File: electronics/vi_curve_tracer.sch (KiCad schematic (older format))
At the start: 56 parts, among them P1 CONN_01X05, P2 USB_OTG, P3 CONN_01X03, P4 CONN_01X03, U1 MCP6004, U2 pic24f08km202, U3 ft230x

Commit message: Fixes #8 - Added ground reference on the terminal block
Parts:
- removed P3: CONN_01X03, kicad_pcb:CONN_1x3_OSTTC032162, symbol CONN_01X03
- removed P4: CONN_01X03, kicad_pcb:CONN_2x3_SOCKET, symbol CONN_01X03
- added P3: CONN_01X04, kicad_pcb:CONN_1x4_OSTTC042162, symbol CONN_01X04
- added P4: CONN_01X06, kicad_pcb:CONN_2x3_SOCKET, symbol CONN_01X06
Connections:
- net GNDD: now also P3.1 (P1)
- net GateVoltage: now also P3.2 (P2), P4.1 (P1), P4.6 (P6)
- net LD_VOLTAGE_0: now also P3.3 (P3), P4.2 (P2), P4.4 (P4)
- net LD_VOLTAGE_1: now also P3.4 (P4), P4.3 (P3), P4.5 (P5)
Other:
- note added: "D"
- note added: "G"
- note added: "S"
- note removed: "TO-220 Socket\nMay want to add extra sockets for different arrangements"
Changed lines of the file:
@@
 encoding utf-8
 Sheet 1 1
-Title ""
-Date ""
-Rev ""
-Comp ""
+Title "Curve Tracer"
+Date "2016-06-06"
+Rev "1.0"
+Comp "for(embed)"
 Comment1 ""
 Comment2 ""
@@
 Text Notes 10200 4450 0    60   ~ 0
 Sense Resistor
-$Comp
-L CONN_01X03 P4
-U 1 1 56B3BE2B
-P 10450 3300
-F 0 "P4" H 10450 3500 50  0000 C CNN
-F 1 "CONN_01X03" V 10550 3300 50  0000 C CNN
-F 2 "kicad_pcb:CONN_2x3_SOCKET" H 10450 3300 50  0001 C CNN
-F 3 "" H 10450 3300 50  0000 C CNN
-F 4 "A06-LC-TT" H 10450 3300 60  0001 C CNN "MPN"
-F 5 "DIP socket" H 10450 3300 60  0001 C CNN "Description"
-F 6 "Assmann WSW Components" H 10450 3300 60  0001 C CNN "Manufacturer"
-	1    10450 3300
-	1    0    0    -1
-$EndComp
-$Comp
-L CONN_01X03 P3
-U 1 1 56B3C6AA
-P 10450 2600
-F 0 "P3" H 10450 2800 50  0000 C CNN
-F 1 "CONN_01X03" V 10550 2600 50  0000 C CNN
-F 2 "kicad_pcb:CONN_1x3_OSTTC032162" H 10450 2600 50  0001 C CNN
-F 3 "" H 10450 2600 50  0000 C CNN
-F 4 "On Shore Technology, Inc." H 10450 2600 60  0001 C CNN "Manufacturer"
-F 5 "terminal block, 5.08mm, 3pos" H 10450 2600 60  0001 C CNN "Description"
-F 6 "OSTTC032162" H 10450 2600 60  0001 C CNN "MPN"
-	1    10450 2600
-	1    0    0    -1
-$EndComp
-Text Notes 10150 3650 0    60   ~ 0
-TO-220 Socket\nMay want to add extra sockets for different arrangements
 Text Notes 10150 2950 0    60   ~ 0
 Screw Terminals
@@
 	4900 2400 5100 2400
 Wire Wire Line
-	7950 3200 10250 3200
+	7950 3200 10550 3200
 Wire Wire Line
 	5000 2700 5000 2750
@@
 	10050 6300 10050 4700
 Wire Wire Line
-	7550 3300 10250 3300
+	7550 3300 10550 3300
 Wire Wire Line
 	10050 2700 10050 4200
 Wire Wire Line
-	10050 3400 10250 3400
+	10050 3400 10550 3400
 Wire Wire Line
 	3850 6900 4000 6900
@@
 Connection ~ 10050 4150
 Wire Wire Line
-	10250 2700 10050 2700
+	10550 2700 10050 2700
 Connection ~ 10050 3400
 Wire Wire Line
-	10250 2600 9900 2600
+	10550 2600 9900 2600
 Wire Wire Line
 	9900 2600 9900 3300
 Connection ~ 9900 3300
 Wire Wire Line
-	10250 2500 9750 2500
+	10550 2500 9750 2500
 Wire Wire Line
 	9750 2500 9750 3200
@@
 Wire Wire Line
 	4350 4600 4450 4600
+$Comp
+L CONN_01X04 P3
+U 1 1 5755D3CE
+P 10750 2550
+F 0 "P3" H 10750 2800 50  0000 C CNN
+F 1 "CONN_01X04" V 10850 2550 50  0000 C CNN
+F 2 "kicad_pcb:CONN_1x4_OSTTC042162" H 10750 2550 50  0001 C CNN
+F 3 "" H 10750 2550 50  0000 C CNN
+F 4 "OSTTC042162" H 10750 2550 60  0001 C CNN "MPN"
+F 5 "On Shore Technology, Inc." H 10750 2550 60  0001 C CNN "Manufacturer"
+F 6 "terminal block, 5.08mm, 4pos" H 10750 2550 60  0001 C CNN "Description"
+	1    10750 2550
+	1    0    0    -1
+$EndComp
+$Comp
+L GNDD #PWR056
+U 1 1 5755DDF7
+P 10450 2400
+F 0 "#PWR056" H 10450 2150 50  0001 C CNN
+F 1 "GNDD" H 10450 2250 50  0000 C CNN
+F 2 "" H 10450 2400 50  0000 C CNN
+F 3 "" H 10450 2400 50  0000 C CNN
+	1    10450 2400
+	0    1    1    0
+$EndComp
+Wire Wire Line
+	10550 2400 10450 2400
+$Comp
+L CONN_01X06 P4
+U 1 1 5755ECF2
+P 10750 3450
+F 0 "P4" H 10750 3800 50  0000 C CNN
+F 1 "CONN_01X06" V 10850 3450 50  0000 C CNN
+F 2 "kicad_pcb:CONN_2x3_SOCKET" H 10750 3450 50  0001 C CNN
+F 3 "" H 10750 3450 50  0000 C CNN
+F 4 "A06-LC-TT" H 10750 3450 60  0001 C CNN "MPN"
+F 5 "DIP socket, 2x3" H 10750 3450 60  0001 C CNN "Description"
+F 6 "Assmann WSW Components" H 10750 3450 60  0001 C CNN "Manufacturer"
+	1    10750 3450
+	1    0    0    -1
+$EndComp
+Text Notes 10950 3250 0    60   ~ 0
+G
+Text Notes 10950 3350 0    60   ~ 0
+D
+Text Notes 10950 3450 0    60   ~ 0
+S
+Text Notes 10950 3750 0    60   ~ 0
+G
+Text Notes 10950 3650 0    60   ~ 0
+S
+Text Notes 10950 3550 0    60   ~ 0
+D
+Wire Wire Line
+	10550 3700 10250 3700
+Wire Wire Line
+	10250 3700 10250 3200
+Connection ~ 10250 3200
+Wire Wire Line
+	10550 3600 10350 3600
+Wire Wire Line
+	10350 3600 10350 3400
+Connection ~ 10350 3400
+Wire Wire Line
+	10550 3500 10450 3500
+Wire Wire Line
+	10450 3500 10450 3300
+Connection ~ 10450 3300
 $EndSCHEMATC

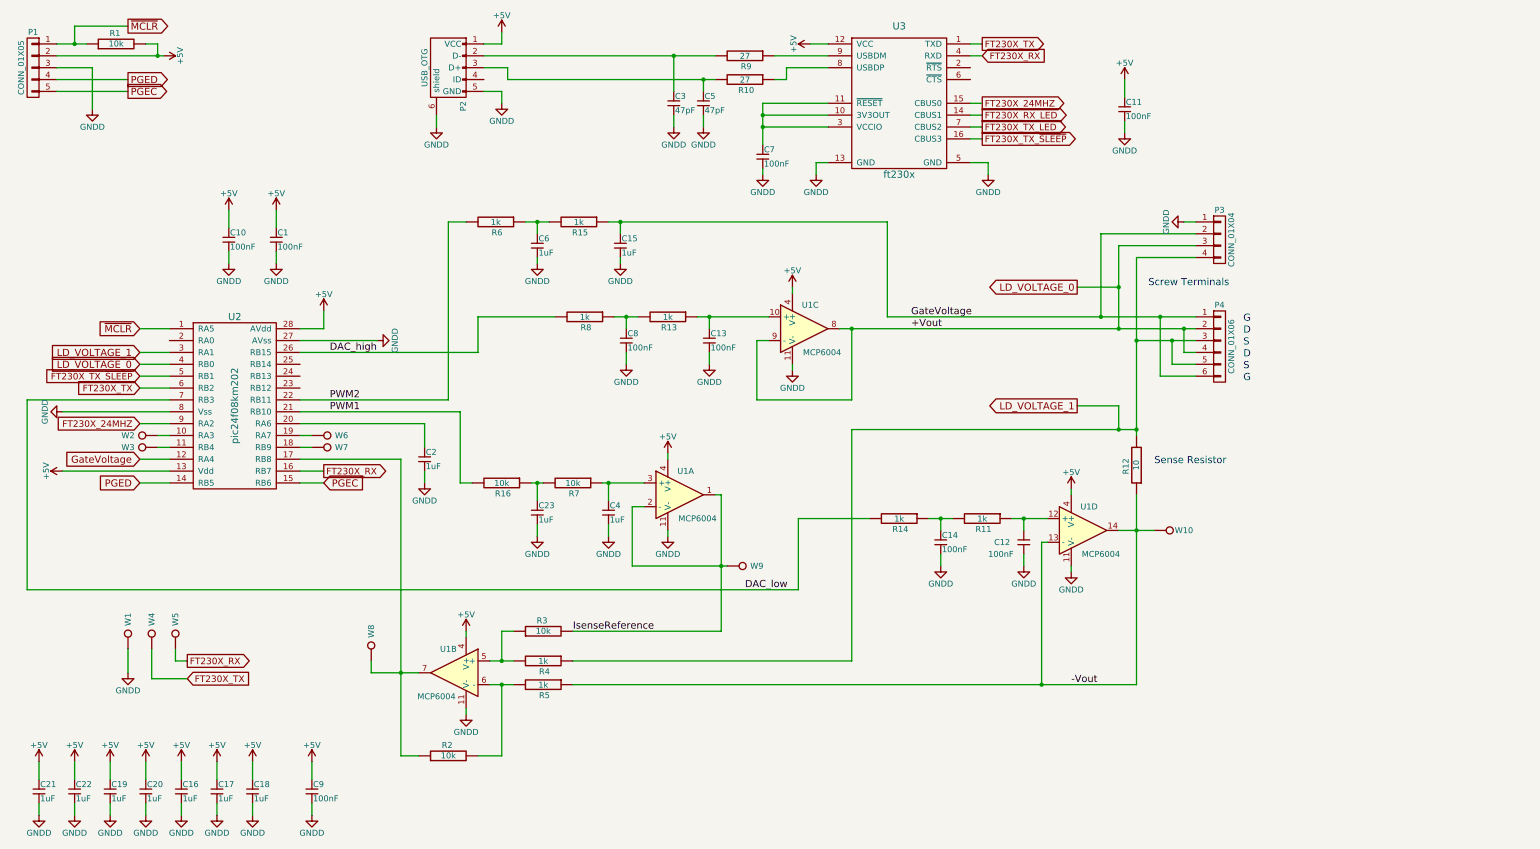
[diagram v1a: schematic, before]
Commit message: See #13 - Added XY outputs to hardware
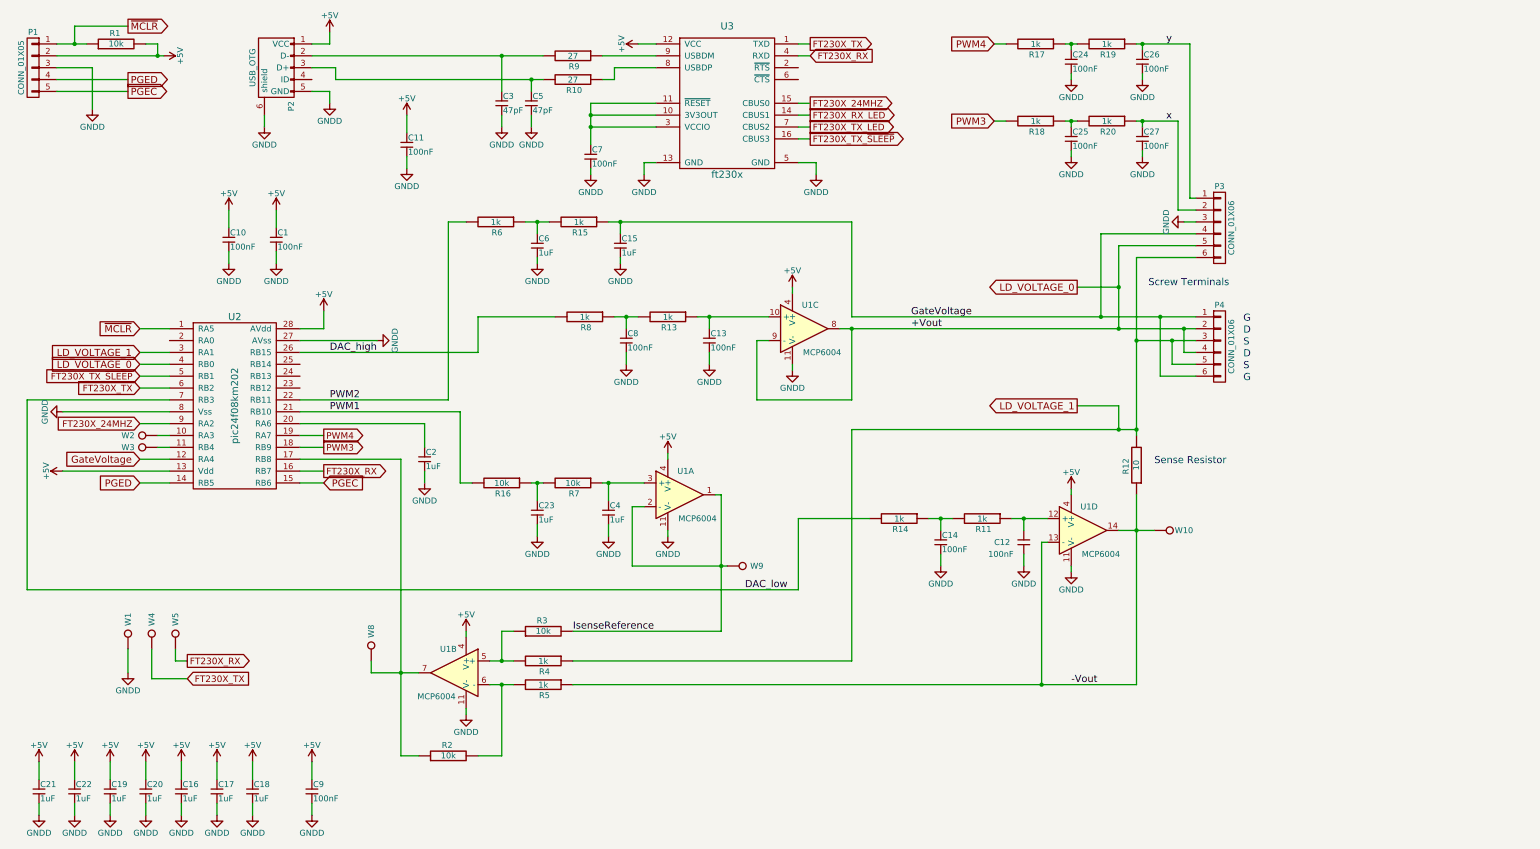
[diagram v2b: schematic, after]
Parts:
- removed P3: CONN_01X04, kicad_pcb:CONN_1x4_OSTTC042162, symbol CONN_01X04
- removed W6, W7: TEST_1P, Measurement_Points:Measurement_Point_Round-SMD-Pad_Small, symbol TEST_1P
- added C24, C25, C26, C27: 100nF, kicad_pcb:SM_0603, symbol Csmall
- added P3: CONN_01X06, kicad_pcb:CONN_1x6_OSTTC062162, symbol CONN_01X06
- added R17, R18, R19, R20: 1k, kicad_pcb:SM_0603, symbol R
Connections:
- net GNDD: now also C24.2, C25.2, C26.2, C27.2, P3.3 (P3)
- net GateVoltage: now also P3.4 (P4)
- net LD_VOLTAGE_0: now also P3.5 (P5)
- net LD_VOLTAGE_1: now also P3.6 (P6)
- net PWM3: now reaches U2.18 (RB9)
- net PWM3: now also R18.2
- net PWM4: now reaches U2.19 (RA7)
- net PWM4: now also R17.2
- new net: C24.1, R17.1, R19.2
- new net: C25.1, R18.1, R20.2
- new net x: C27.1, P3.2 (P2), R20.1
- new net y: C26.1, P3.1 (P1), R19.1
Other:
- moved on the sheet: C11, C3, C5, C7, P2, R10, R9, U3

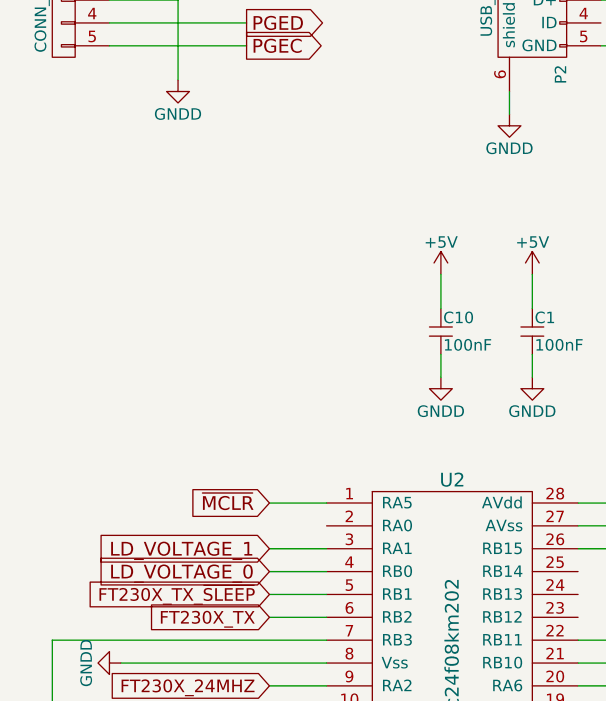
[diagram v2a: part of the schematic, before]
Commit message: Added extra header to short in case we want to add a bootloader later
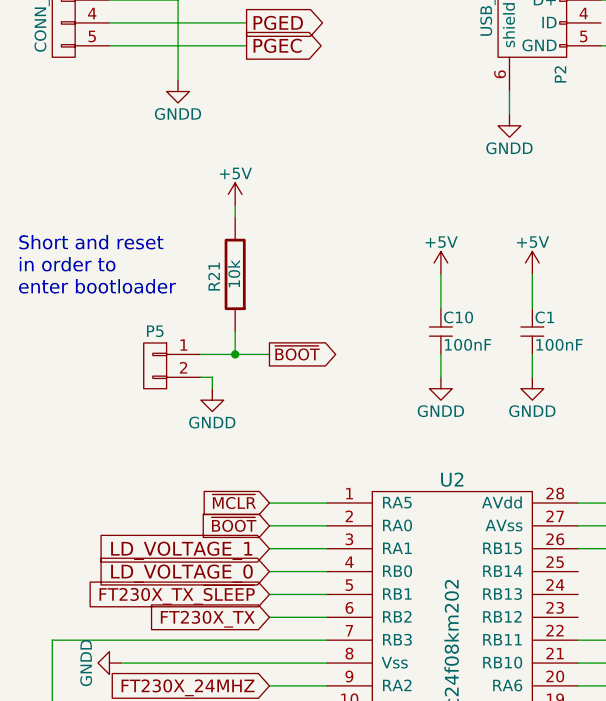
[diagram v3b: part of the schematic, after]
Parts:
- added P5: CONN_01X02, Pin_Headers:Pin_Header_Straight_1x02, symbol CONN_01X02
- added R21: 10k, kicad_pcb:SM_0603, symbol R
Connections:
- net +5V: now also R21.2
- net GNDD: now also P5.2 (P2)
- net ~BOOT: now reaches U2.2 (RA0)
- net ~BOOT: now also P5.1 (P1), R21.1
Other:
- note added: "Short and reset\nin order to\nenter bootloader"
